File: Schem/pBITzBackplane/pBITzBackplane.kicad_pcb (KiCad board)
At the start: 4 copper layers, 243.8 x 243.8 mm, 54 parts, among them J1 ATX-24, J2 pBITzBus, J3 pBITzBus, J4 pBITzBus, J5 pBITzBus, J6 pBITzBus, J7 Conn_02x10_Odd_Even, Q1 BSS138, SW1 SW_Push, U1 ATtiny85-20P

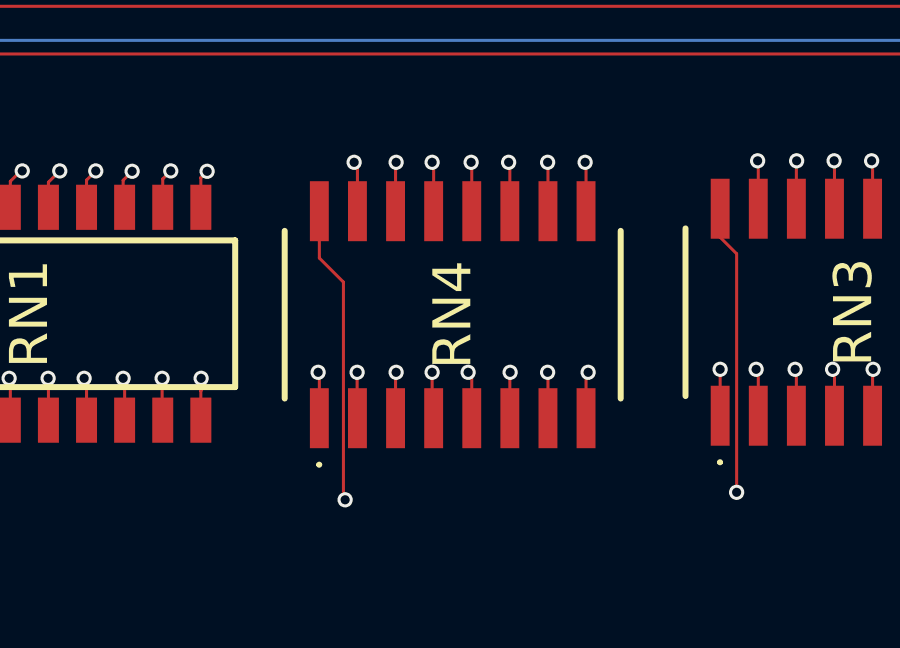
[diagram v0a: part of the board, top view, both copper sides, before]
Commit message: Just regenerated the PDF of the schematics and the images of the board
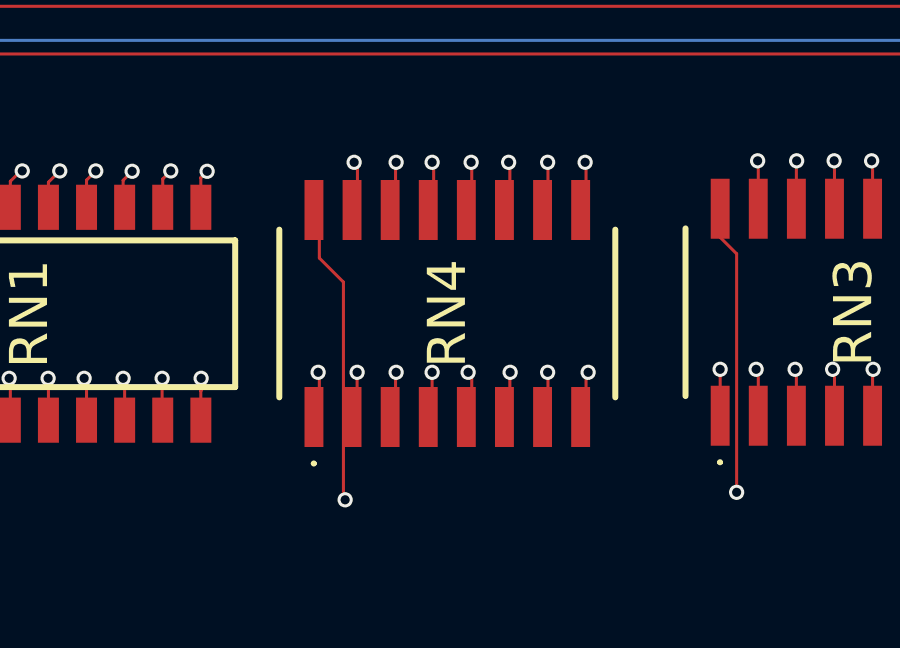
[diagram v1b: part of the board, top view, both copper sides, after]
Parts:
- moved RN4 0.18 mm to (309.8, 292.1)
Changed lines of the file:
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@@
 	(footprint "Footprints:4816PT02472LF"
 		(layer "F.Cu")
-		(at 309.957015 292.099695 90)
+		(at 309.776857 292.059893 90)
 		(descr "4816P-T02-472LF-1")
 		(tags "Resistor Network")
@@
 			)
 		)
+		(model "${PBITZ_ROOT}/99-KiCad-Lib/3D-Models/4816p.stp"
+			(offset
+				(xyz 0 1.27 0)
+			)
+			(scale
+				(xyz 1 1 1)
+			)
+			(rotate
+				(xyz -90 -0 -0)
+			)
+		)
 	)
 	(footprint "Package_DIP:DIP-8_W7.62mm"
@@
 	)
 	(zone
-		(net "+5V_AON")
+		(net "GND")
 		(layer "F.Cu")
 		(hatch none 0.1)
-		(priority 30000)
+		(priority 30001)
 		(attr
 			(teardrop
@@
 		(polygon
 			(pts
-				(xy 347.731596 394.9568) (xy 347.731596 394.8552) (xy 347.285173 394.674004) (xy 347.230596 394.906)
-				(xy 347.375293 395.127067)
+				(xy 353.243604 382.0922) (xy 353.243604 382.1938) (xy 353.599907 382.350867) (xy 353.744604 382.143)
+				(xy 353.599907 381.935133)
 			)
 		)
@@
 	)
 	(zone
-		(net "GND")
+		(net "+5V_AON")
 		(layer "F.Cu")
 		(hatch none 0.1)
-		(priority 30001)
+		(priority 30000)
 		(attr
 			(teardrop
@@
 		(polygon
 			(pts
-				(xy 353.243604 382.0922) (xy 353.243604 382.1938) (xy 353.599907 382.350867) (xy 353.744604 382.143)
-				(xy 353.599907 381.935133)
+				(xy 347.731596 394.9568) (xy 347.731596 394.8552) (xy 347.285173 394.674004) (xy 347.230596 394.906)
+				(xy 347.375293 395.127067)
 			)
 		)
 	)
 	(zone
-		(net "GND")
+		(net "+5V_AON")
 		(layer "F.Cu")
 		(hatch none 0.1)
-		(priority 30002)
+		(priority 30003)
 		(attr
 			(teardrop
@@
 		(polygon
 			(pts
-				(xy 340.8102 381.520596) (xy 340.9118 381.520596) (xy 341.068867 381.164293) (xy 340.861 381.019596)
-				(xy 340.653133 381.164293)
+				(xy 341.076796 393.3444) (xy 341.076796 393.2428) (xy 340.720493 393.085733) (xy 340.575796 393.2936)
+				(xy 340.720493 393.501467)
 			)
 		)
 	)
 	(zone
-		(net "+5V_AON")
+		(net "GND")
 		(layer "F.Cu")
 		(hatch none 0.1)
-		(priority 30003)
+		(priority 30002)
 		(attr
 			(teardrop
@@
 		(polygon
 			(pts
-				(xy 341.076796 393.3444) (xy 341.076796 393.2428) (xy 340.720493 393.085733) (xy 340.575796 393.2936)
-				(xy 340.720493 393.501467)
+				(xy 340.8102 381.520596) (xy 340.9118 381.520596) (xy 341.068867 381.164293) (xy 340.861 381.019596)
+				(xy 340.653133 381.164293)
 			)
 		)
@@
 		(layer "In2.Cu")
 		(hatch none 0.1)
-		(priority 30005)
+		(priority 30001)
 		(attr
 			(teardrop
@@
 		(polygon
 			(pts
-				(xy 340.607 392.820286) (xy 340.353 392.820286) (xy 340.6284 393.04802) (xy 340.48 393.321286) (xy 340.3316 393.2936)
+				(xy 347.1094 395.414396) (xy 347.3634 395.414396) (xy 347.481596 394.967973) (xy 347.2364 394.913396)
+				(xy 346.991204 394.967973)
 			)
 		)
@@
 		(layer "In2.Cu")
 		(hatch none 0.1)
-		(priority 30001)
+		(priority 30004)
 		(attr
 			(teardrop
@@
 		(polygon
 			(pts
-				(xy 347.1094 395.414396) (xy 347.3634 395.414396) (xy 347.481596 394.967973) (xy 347.2364 394.913396)
-				(xy 346.991204 394.967973)
+				(xy 340.963136 393.695) (xy 340.963136 393.441) (xy 340.945803 393.478197) (xy 340.789467 393.154707)
+				(xy 340.577496 393.289496) (xy 340.442707 393.501467) (xy 340.766197 393.657803) (xy 340.856 393.695)
 			)
 		)
@@
 		(layer "In2.Cu")
 		(hatch none 0.1)
-		(priority 30004)
+		(priority 30003)
 		(attr
 			(teardrop
@@
 		(polygon
 			(pts
-				(xy 340.963136 393.695) (xy 340.963136 393.441) (xy 340.945803 393.478197) (xy 340.789467 393.154707)
-				(xy 340.577496 393.289496) (xy 340.442707 393.501467) (xy 340.766197 393.657803) (xy 340.856 393.695)
+				(xy 347.3634 394.424004) (xy 347.1094 394.424004) (xy 346.991204 394.870427) (xy 347.2364 394.925004)
+				(xy 347.481596 394.870427)
+			)
+		)
+	)
+	(zone
+		(net "+5V_AON")
+		(layer "In2.Cu")
+		(hatch none 0.1)
+		(priority 30000)
+		(attr
+			(teardrop
+				(type padvia)
+			)
+		)
+		(connect_pads yes
+			(clearance 0)
+		)
+		(min_thickness 0.0254)
+		(fill yes
+			(island_removal_mode 1)
+		)
+		(polygon
+			(pts
+				(xy 340.497241 385.019554) (xy 340.676846 385.199159) (xy 341.076093 384.967067) (xy 340.941304 384.755096)
+				(xy 340.729333 384.620307)
 			)
 		)
@@
 		(layer "In2.Cu")
 		(hatch none 0.1)
-		(priority 30003)
+		(priority 30005)
 		(attr
 			(teardrop
@@
 		(polygon
 			(pts
-				(xy 347.3634 394.424004) (xy 347.1094 394.424004) (xy 346.991204 394.870427) (xy 347.2364 394.925004)
-				(xy 347.481596 394.870427)
+				(xy 340.607 392.820286) (xy 340.353 392.820286) (xy 340.6284 393.04802) (xy 340.48 393.321286) (xy 340.3316 393.2936)
 			)
 		)
@@
 			)
 		)
-	)
-	(zone
-		(net "+5V_AON")
-		(layer "In2.Cu")
-		(hatch none 0.1)
-		(priority 30000)
-		(attr
-			(teardrop
-				(type padvia)
-			)
-		)
-		(connect_pads yes
-			(clearance 0)
-		)
-		(min_thickness 0.0254)
-		(fill yes
-			(island_removal_mode 1)
-		)
-		(polygon
-			(pts
-				(xy 340.497241 385.019554) (xy 340.676846 385.199159) (xy 341.076093 384.967067) (xy 340.941304 384.755096)
-				(xy 340.729333 384.620307)
-			)
-		)
